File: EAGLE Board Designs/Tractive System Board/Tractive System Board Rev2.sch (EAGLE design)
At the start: 134 parts, among them J3 CONNECTOR-8_MF_T_V_, J5 CONNECTOR-4__, K4 RELAY_SPST_NC_POLARIZED_D_12, K5 RELAY_SPST_NO_D_12, Q2 TRANSISTOR_N_MOS__PMV15ENEA, U1 LTC6994_1, U10 DCM4623TD2J13D0T70, U11 RELAY_SOLIDSTATE_NC_AG, U15 LOGICGATE_INVERTER_DCKR, U16 LTC3639, U17 VOLTAGE_REGULATOR_ADJ_LR8_DPAK, U18 ISO224B_AIRGAP, U19 ISO224B_AIRGAP, U2 VOLTAGE_REGULATOR_SOT223_5V

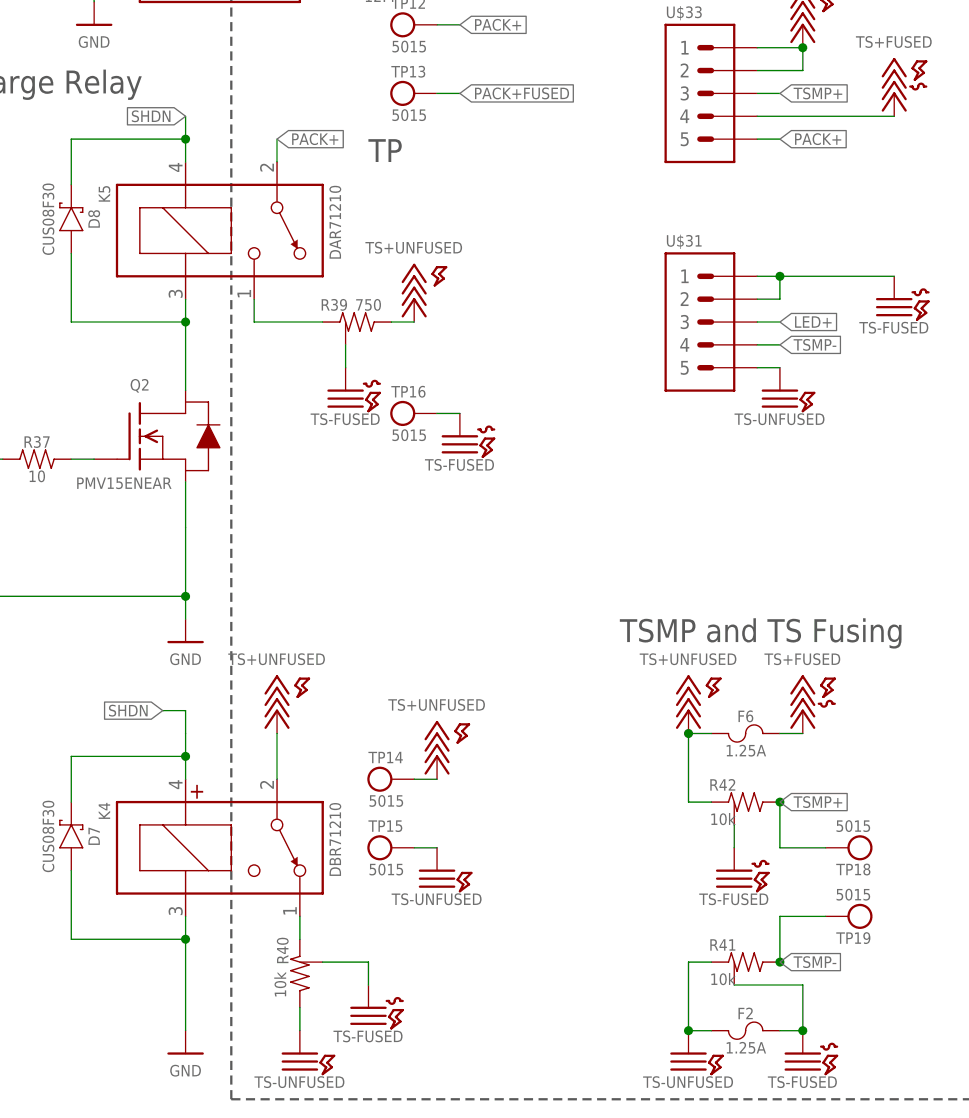
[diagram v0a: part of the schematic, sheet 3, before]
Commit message: Made the major schematic and board design changes needed for the last rev
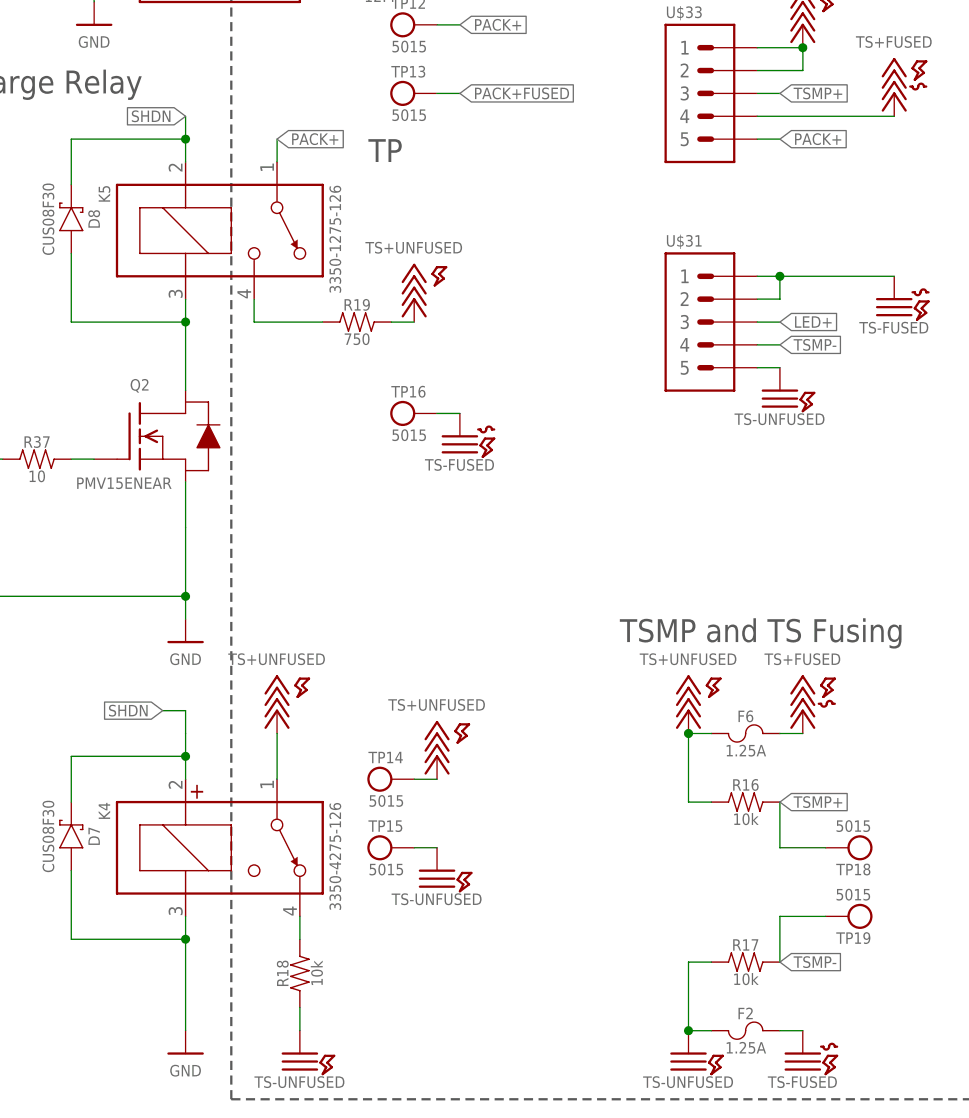
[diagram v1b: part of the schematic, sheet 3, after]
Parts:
- removed R39: RESISTOR_GND_750, HyTechDevicesTempTSB:RESISTOR_GND_750
- removed R40, R41, R42: RESISTOR_GND_10K, HyTechDevicesTempTSB:RESISTOR_GND_10K
- added D14: RECTIFIER_400V_SOD123, HyTechDevicesTempTSB:RECTIFIER_400V_SOD123
- added R16, R17, R18: RESISTOR_B20_10K, HyTechDevices:RESISTOR_B20_10K
- added R19: RESISTOR_B20_750, HyTechDevices:RESISTOR_B20_750
- J3: value CONNECTOR-8_MF_T_V_ -> CONNECTOR-8__; device HyTechDevices:CONNECTOR-8_MF_T_V_ -> HyTechDevices:CONNECTOR-8__
- K4: value RELAY_SPST_NC_POLARIZED_D_12 -> RELAY_SPST_NC_POLARIZED_3550_12; device HyTechDevices:RELAY_SPST_NC_POLARIZED_D_12 -> HyTechDevices:RELAY_SPST_NC_POLARIZED_3550_12
- K5: value RELAY_SPST_NO_D_12 -> RELAY_SPST_NO_3550_12; device HyTechDevices:RELAY_SPST_NO_D_12 -> HyTechDevices:RELAY_SPST_NO_3550_12
- R43: value RESISTOR_0805_365K -> RESISTOR_0805_HV365K; device HyTechDevices:RESISTOR_0805_365K -> HyTechDevices:RESISTOR_0805_HV365K
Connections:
- net N$15: now also D14.C
- net N$50: now also R19.1; no longer R39.1
- net N$51: now also R18.2; no longer R40.1
- net N$58: now also D14.A
- net TS+UNFUSED: now also R16.1, R19.2; no longer R39.2, R42.1
- net TS-FUSED: no longer R39.3, R40.3, R41.3, R42.3
- net TS-UNFUSED: now also R17.1, R18.1; no longer R40.2, R41.1
- net TSMP+: now also R16.2; no longer R42.2
- net TSMP-: now also R17.2; no longer R41.2

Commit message: Made final changes to schematic
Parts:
- D12: value LED_0603_WHITE -> LED_0603_ORANGE; device HyTechDevices:LED_0603_WHITE -> HyTechDevices:LED_0603_ORANGE
- D2: value LED_0603_ORANGE -> LED_0603_WHITE; device HyTechDevices:LED_0603_ORANGE -> HyTechDevices:LED_0603_WHITE
- D3: value LED_0603_YELLOW -> LED_0603_GREEN; device HyTechDevices:LED_0603_YELLOW -> HyTechDevices:LED_0603_GREEN
- D5: value LED_0603_WHITE -> LED_2835_BLUE; device HyTechDevices:LED_0603_WHITE -> HyTechDevices:LED_2835_BLUE
- R26: value RESISTOR_0805_1 -> RESISTOR_0603_3.3; device HyTechDevices:RESISTOR_0805_1 -> HyTechDevices:RESISTOR_0603_3.3
- R27: value RESISTOR_0805_12.4 -> RESISTOR_0603_3.3; device HyTechDevices:RESISTOR_0805_12.4 -> HyTechDevices:RESISTOR_0603_3.3
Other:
- note added: "10A Mini-Blade Fuse"
- note added: "Molex Microfit 4-pin"
- note added: "Molex Microfit 6-pin, spaced"
- note added: "Molex Microfit 7-pin, spaced"
- note added: "Shunt resistor rated to 174 mA"
- note removed: "1 ohm 1/8 W shunt resistor"
- note removed: "1 ohm 1/8W shunt resistor"

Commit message: Final changes to both
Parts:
- D5: value LED_2835_BLUE -> LED_0603_BLUE; device HyTechDevices:LED_2835_BLUE -> HyTechDevices:LED_0603_BLUE
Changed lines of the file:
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@@
 <part name="TP11" library="HyTechDevices" deviceset="TEST_POINT" device=""/>
 <part name="R30" library="HyTechDevices" deviceset="RESISTOR_?_*" device="0603" technology="1K"/>
-<part name="D5" library="HyTechDevices" deviceset="LED_?_*" device="2835" technology="BLUE" value="LED_2835_BLUE"/>
+<part name="D5" library="HyTechDevices" deviceset="LED_?_*" device="0603" technology="BLUE" value="LED_0603_BLUE"/>
 <part name="D9" library="HyTechDevices" deviceset="LED_?_*" device="0603" technology="BLUE"/>
 <part name="R35" library="HyTechDevices" deviceset="RESISTOR_?_*" device="0603" technology="1K"/>

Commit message: Fixed externals
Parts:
- D4: value LED_0603_GREEN -> LED_0603_YELLOW; device HyTechDevices:LED_0603_GREEN -> HyTechDevices:LED_0603_YELLOW
- J3: value CONNECTOR-8__ -> CONNECTOR-8_S_S; device HyTechDevices:CONNECTOR-8__ -> HyTechDevices:CONNECTOR-8_S_S
- L4: value INDUCTOR_PA4334_3.6UH -> INDUCTOR_74451133_3.6UH; device HyTechDevices:INDUCTOR_PA4334_3.6UH -> HyTechDevices:INDUCTOR_74451133_3.6UH
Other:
- note added: "Flex Stack Board Connector"
- moved on the sheet: O25
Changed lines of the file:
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@@
 <part name="R32" library="HyTechDevices" deviceset="RESISTOR_?_*" device="0603" technology="1K"/>
 <part name="R33" library="HyTechDevices" deviceset="RESISTOR_?_*" device="0603" technology="DNP"/>
-<part name="L4" library="HyTechDevices" deviceset="INDUCTOR_?_*" device="PA4334" technology="3.6UH"/>
+<part name="L4" library="HyTechDevices" deviceset="INDUCTOR_?_*" device="74451133" technology="3.6UH" value="INDUCTOR_74451133_3.6UH"/>
 <part name="L5" library="HyTechDevices" deviceset="INDUCTOR_?_*" device="WELMHI" technology="56UH"/>
 <part name="D6" library="HyTechDevices" deviceset="LED_?_*" device="0603" technology="RED"/>
@@
 <part name="P36" library="HyTechSupplies" deviceset="TS+UNFUSED" device=""/>
 <part name="P37" library="HyTechSupplies" deviceset="GND" device=""/>
-<part name="J3" library="HyTechDevices" deviceset="CONNECTOR-8_?_*" device=""/>
+<part name="J3" library="HyTechDevices" deviceset="CONNECTOR-8_?_*" device="S" technology="S"/>
 <part name="P39" library="HyTechSupplies" deviceset="GND" device=""/>
 <part name="U$32" library="HyTechSupplies" deviceset="TS+FUSED" device=""/>
@@
 <part name="D3" library="HyTechDevices" deviceset="LED_?_*" device="0603" technology="GREEN" value="LED_0603_GREEN"/>
 <part name="R52" library="HyTechDevices" deviceset="RESISTOR_?_*" device="0603" technology="1K"/>
-<part name="D4" library="HyTechDevices" deviceset="LED_?_*" device="0603" technology="GREEN"/>
+<part name="D4" library="HyTechDevices" deviceset="LED_?_*" device="0603" technology="YELLOW" value="LED_0603_YELLOW"/>
 <part name="D11" library="HyTechDevices" deviceset="LED_?_*" device="0603" technology="BLUE"/>
 <part name="R53" library="HyTechDevices" deviceset="RESISTOR_?_*" device="0603" technology="1K"/>
@@
 <part name="R19" library="HyTechDevices" deviceset="RESISTOR_?_*" device="B20" technology="750"/>
 <part name="D14" library="HyTechDevicesTempTSB" deviceset="RECTIFIER_*_?" device="SOD123" technology="400V"/>
-<part name="U$49" library="HyTechFrames" deviceset="FRAME_SCHEMATIC_ONLY" device=""/>
+<part name="U$49" library="HyTechFrames" deviceset="FRAME_SCHEMATIC_ONLY" device="">
+<attribute name="DESCRIPTION_1" value="Externals Sheet"/>
+<attribute name="ENGINEER" value="Cody Kaminsky"/>
+</part>
 <part name="O9" library="HyTechExternal" deviceset="CRIMP_*" device="" technology="MICROFIT_20-24"/>
 <part name="O10" library="HyTechExternal" deviceset="CRIMP_*" device="" technology="MICROFIT_20-24"/>
@@
 <part name="O22" library="HyTechExternal" deviceset="CRIMP_*" device="" technology="MICROFIT_20-24"/>
 <part name="O23" library="HyTechExternal" deviceset="RECEPTACLE-4_*" device="" technology="MICROFIT"/>
-<part name="U$50" library="HyTechExternal" deviceset="RECEPTACLE-6_SINGLE_*" device="" technology="MICROFIT"/>
-<part name="U$51" library="HyTechExternal" deviceset="RECEPTACLE-7_*" device="" technology="MICROFIT"/>
 <part name="O25" library="HyTechExternal" deviceset="FUSE_*" device="" technology="MINI_BLADE_10"/>
+<part name="O1" library="HyTechExternal" deviceset="RECEPTACLE-8_*" device="" technology="FLEXSTACK"/>
+<part name="O2" library="HyTechExternal" deviceset="RECEPTACLE-7_*" device="" technology="MICROFIT"/>
+<part name="O3" library="HyTechExternal" deviceset="RECEPTACLE-6_SINGLE_*" device="" technology="MICROFIT"/>
 </parts>
 <sheets>
@@
 <net name="TS+FUSED" class="0">
 <segment>
-<pinref part="U$2" gate="G$1" pin="TS+"/>
+<pinref part="U$2" gate="G$1" pin="TS+FUSED"/>
 <pinref part="R26" gate="G$1" pin="1"/>
 <wire x1="66.04" y1="198.12" x2="68.58" y2="198.12" width="0.6096" layer="91"/>
 </segment>
 <segment>
-<pinref part="U$40" gate="G$1" pin="TS+"/>
+<pinref part="U$40" gate="G$1" pin="TS+FUSED"/>
 <wire x1="50.8" y1="149.86" x2="50.8" y2="152.4" width="0.6096" layer="91"/>
 <pinref part="R1" gate="G$1" pin="2"/>
@@
 <wire x1="48.26" y1="167.64" x2="43.18" y2="167.64" width="0.6096" layer="91"/>
 <junction x="48.26" y="167.64"/>
-<pinref part="U$27" gate="G$1" pin="TS+"/>
+<pinref part="U$27" gate="G$1" pin="TS+FUSED"/>
 </segment>
 </net>
@@
 <pinref part="F6" gate="G$1" pin="2"/>
 <wire x1="243.84" y1="101.6" x2="246.38" y2="101.6" width="0.6096" layer="91"/>
-<pinref part="U$36" gate="G$1" pin="TS+"/>
-</segment>
-<segment>
-<pinref part="U$32" gate="G$1" pin="TS+"/>
+<pinref part="U$36" gate="G$1" pin="TS+FUSED"/>
+</segment>
+<segment>
+<pinref part="U$32" gate="G$1" pin="TS+FUSED"/>
 <wire x1="241.3" y1="170.18" x2="256.54" y2="170.18" width="0.6096" layer="91"/>
 <pinref part="U$33" gate="G$1" pin="4"/>
@@
 <text x="152.4" y="198.12" size="1.778" layer="97">Molex Microfit 6-pin, spaced</text>
 <text x="193.04" y="198.12" size="1.778" layer="97">Molex Microfit 7-pin, spaced</text>
+<text x="63.5" y="190.5" size="1.778" layer="97">Flex Stack Board Connector</text>
 </plain>
 <instances>
@@
 </instance>
 <instance part="O10" gate="G$1" x="109.22" y="182.88" smashed="yes">
-<attribute name="MPN" x="109.22" y="179.578" size="1.27" layer="96" align="top-left"/>
 <attribute name="NAME" x="109.22" y="183.642" size="1.27" layer="95"/>
 </instance>
 <instance part="O11" gate="G$1" x="114.3" y="182.88" smashed="yes">
-<attribute name="MPN" x="114.3" y="179.578" size="1.27" layer="96" align="top-left"/>
 <attribute name="NAME" x="114.3" y="183.642" size="1.27" layer="95"/>
 </instance>
 <instance part="O12" gate="G$1" x="119.38" y="182.88" smashed="yes">
-<attribute name="MPN" x="119.38" y="179.578" size="1.27" layer="96" align="top-left"/>
 <attribute name="NAME" x="119.38" y="183.642" size="1.27" layer="95"/>
 </instance>
@@
 </instance>
 <instance part="O14" gate="G$1" x="157.48" y="182.88" smashed="yes">
-<attribute name="MPN" x="157.48" y="179.578" size="1.27" layer="96" align="top-left"/>
 <attribute name="NAME" x="157.48" y="183.642" size="1.27" layer="95"/>
 </instance>
 <instance part="O15" gate="G$1" x="162.56" y="182.88" smashed="yes">
-<attribute name="MPN" x="162.56" y="179.578" size="1.27" layer="96" align="top-left"/>
 <attribute name="NAME" x="162.56" y="183.642" size="1.27" layer="95"/>
 </instance>
 <instance part="O16" gate="G$1" x="167.64" y="182.88" smashed="yes">
-<attribute name="MPN" x="167.64" y="179.578" size="1.27" layer="96" align="top-left"/>
 <attribute name="NAME" x="167.64" y="183.642" size="1.27" layer="95"/>
 </instance>
 <instance part="O17" gate="G$1" x="172.72" y="182.88" smashed="yes">
-<attribute name="MPN" x="172.72" y="179.578" size="1.27" layer="96" align="top-left"/>
 <attribute name="NAME" x="172.72" y="183.642" size="1.27" layer="95"/>
 </instance>
@@
 </instance>
 <instance part="O19" gate="G$1" x="198.12" y="182.88" smashed="yes">
-<attribute name="MPN" x="198.12" y="179.578" size="1.27" layer="96" align="top-left"/>
 <attribute name="NAME" x="198.12" y="183.642" size="1.27" layer="95"/>
 </instance>
 <instance part="O20" gate="G$1" x="203.2" y="182.88" smashed="yes">
-<attribute name="MPN" x="203.2" y="179.578" size="1.27" layer="96" align="top-left"/>
 <attribute name="NAME" x="203.2" y="183.642" size="1.27" layer="95"/>
 </instance>
 <instance part="O21" gate="G$1" x="208.28" y="182.88" smashed="yes">
-<attribute name="MPN" x="208.28" y="179.578" size="1.27" layer="96" align="top-left"/>
 <attribute name="NAME" x="208.28" y="183.642" size="1.27" layer="95"/>
 </instance>
 <instance part="O22" gate="G$1" x="213.36" y="182.88" smashed="yes">
-<attribute name="MPN" x="213.36" y="179.578" size="1.27" layer="96" align="top-left"/>
 <attribute name="NAME" x="213.36" y="183.642" size="1.27" layer="95"/>
 </instance>
@@
 <attribute name="NAME" x="104.14" y="191.262" size="1.27" layer="95"/>
 </instance>
-<instance part="U$50" gate="G$1" x="152.4" y="190.5" smashed="yes">
+<instance part="O25" gate="G$1" x="38.1" y="182.88" smashed="yes">
+<attribute name="MPN" x="38.1" y="179.578" size="1.27" layer="96" align="top-left"/>
+<attribute name="NAME" x="38.1" y="183.642" size="1.27" layer="95"/>
+</instance>
+<instance part="O1" gate="G$1" x="71.12" y="182.88" smashed="yes">
+<attribute name="MPN" x="71.12" y="179.578" size="1.27" layer="96" align="top-left"/>
+<attribute name="NAME" x="71.12" y="183.642" size="1.27" layer="95"/>
+</instance>
+<instance part="O2" gate="G$1" x="193.04" y="190.5" smashed="yes">
+<attribute name="MPN" x="193.04" y="187.198" size="1.27" layer="96" align="top-left"/>
+<attribute name="NAME" x="193.04" y="191.262" size="1.27" layer="95"/>
+</instance>
+<instance part="O3" gate="G$1" x="152.4" y="190.5" smashed="yes">
 <attribute name="MPN" x="152.4" y="187.198" size="1.27" layer="96" align="top-left"/>
 <attribute name="NAME" x="152.4" y="191.262" size="1.27" layer="95"/>
 </instance>
-<instance part="U$51" gate="G$1" x="193.04" y="190.5" smashed="yes">
-<attribute name="MPN" x="193.04" y="187.198" size="1.27" layer="96" align="top-left"/>
-<attribute name="NAME" x="193.04" y="191.262" size="1.27" layer="95"/>
-</instance>
-<instance part="O25" gate="G$1" x="38.1" y="180.34" smashed="yes">
-<attribute name="MPN" x="38.1" y="177.038" size="1.27" layer="96" align="top-left"/>
-<attribute name="NAME" x="38.1" y="181.102" size="1.27" layer="95"/>
-</instance>
 </instances>

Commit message: Made final board changes
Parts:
- U$1: value RELAY_SOLIDSTATE_NO_AG -> RELAY_SOLIDSTATE_NO; device HyTechDevicesTempTSB:RELAY_SOLIDSTATE_NO_AG -> HyTechDevices:RELAY_SOLIDSTATE_NO
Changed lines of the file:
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@@
 <layer number="155" name="FabDoc3" color="7" fill="1" visible="no" active="yes"/>
 <layer number="156" name="HVSpacing" color="12" fill="1" visible="no" active="yes"/>
+<layer number="157" name="HIGH_VOLTAGE_WIRES" color="2" fill="1" visible="yes" active="yes"/>
 <layer number="191" name="mNets" color="7" fill="1" visible="no" active="yes"/>
 <layer number="192" name="mBusses" color="7" fill="1" visible="no" active="yes"/>
@@
 <part name="C4" library="HyTechDevices" deviceset="CAPACITOR_?_*" device="1206" technology="250V_0.1UF"/>
 <part name="J5" library="HyTechDevices" deviceset="CONNECTOR-4_?_*" device=""/>
-<part name="U$1" library="HyTechDevicesTempTSB" deviceset="RELAY_SOLIDSTATE_NO_?" device="AG"/>
+<part name="U$1" library="HyTechDevices" deviceset="RELAY_SOLIDSTATE_NO" device=""/>
 <part name="U$2" library="HyTechSupplies" deviceset="TS+FUSED" device=""/>
 <part name="D1" library="HyTechDevices" deviceset="TVS_*" device="" technology="8V" value="TVS_8V"/>
